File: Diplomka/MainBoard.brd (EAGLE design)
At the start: 100 x 100 mm, 44 parts, among them K1 ARK550/2, Q1 AP2012P3C-P22, Q2 BC817-40LT1SMD, Q3 SS8050-G, Q4 SS8050-G, U1 ESP32-WROOM-32, U2 AMS1117-3.3

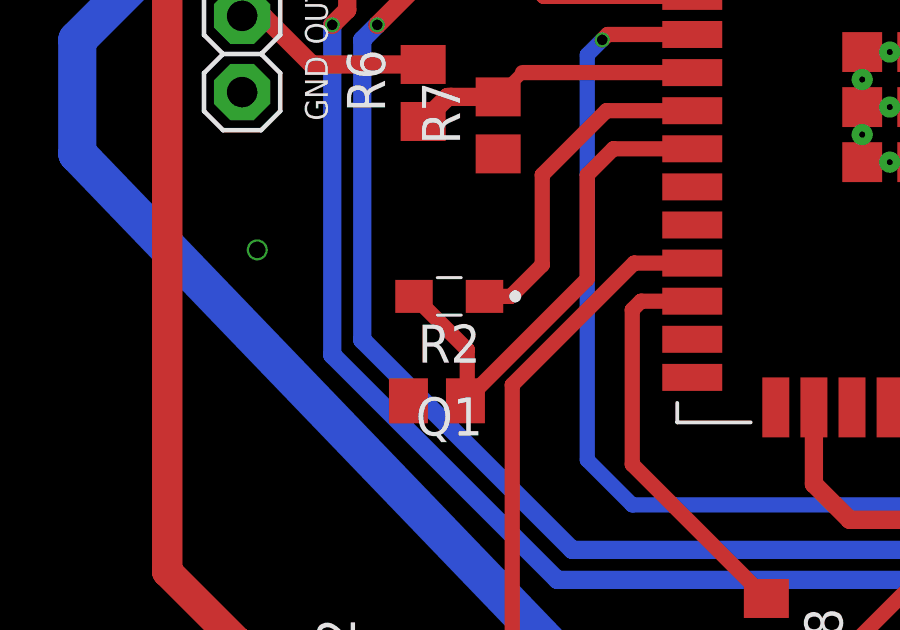
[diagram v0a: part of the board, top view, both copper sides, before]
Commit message: Přidán rozumný fototranzistor.
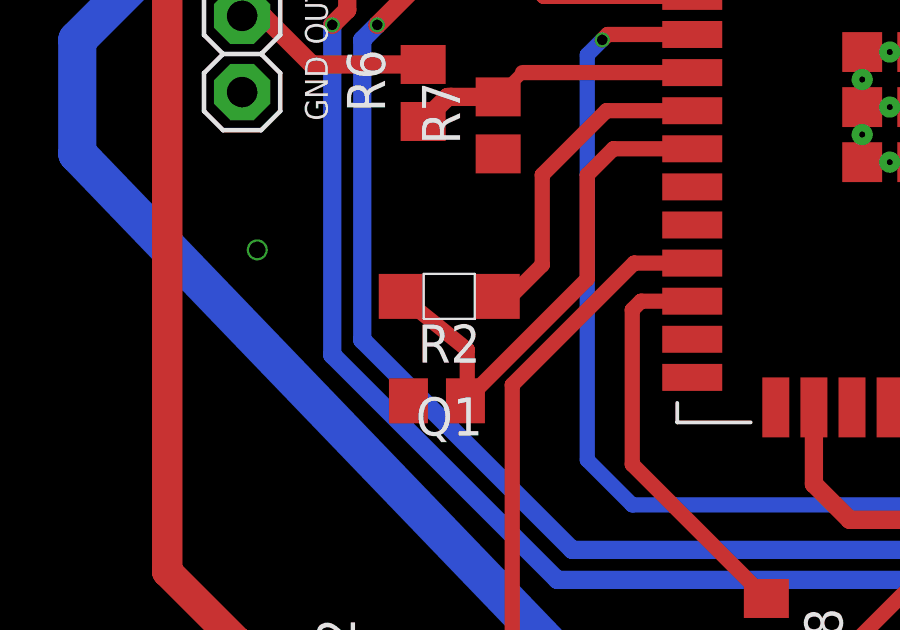
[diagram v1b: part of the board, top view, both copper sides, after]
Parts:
- Q1: value AP2012P3C-P22 -> PT15-21C/TR8; device SamacSys_Parts:AP2012P3CP22 -> myParts:PT15-21C/TR8
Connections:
- net PHOTOTRAN: now also Q1.E; no longer Q1.2
- net PHOTOTRAN_CONTROL: now also Q1.C; no longer Q1.1
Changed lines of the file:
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@@
 <grid distance="1" unitdist="mm" unit="mm" style="lines" multiple="1" display="yes" altdistance="5" altunitdist="mil" altunit="mil"/>
 <layers>
-<layer number="1" name="Top" color="4" fill="1" visible="no" active="yes"/>
+<layer number="1" name="Top" color="4" fill="1" visible="yes" active="yes"/>
 <layer number="2" name="Route2" color="1" fill="3" visible="no" active="no"/>
 <layer number="3" name="Route3" color="4" fill="3" visible="no" active="no"/>
@@
 <layer number="14" name="Route14" color="1" fill="6" visible="no" active="no"/>
 <layer number="15" name="Route15" color="4" fill="6" visible="no" active="no"/>
-<layer number="16" name="Bottom" color="1" fill="1" visible="no" active="yes"/>
+<layer number="16" name="Bottom" color="1" fill="1" visible="yes" active="yes"/>
 <layer number="17" name="Pads" color="2" fill="1" visible="yes" active="yes"/>
 <layer number="18" name="Vias" color="2" fill="1" visible="yes" active="yes"/>
@@
 <attribute name="VALUE" x="58.93" y="19.27" size="1.27" layer="27" rot="R270"/>
 </element>
-<element name="Q1" library="SamacSys_Parts" package="AP2012P3CP22" value="AP2012P3C-P22" x="33.4" y="41.45" smashed="yes" rot="R180">
-<attribute name="DESCRIPTION" value="Phototransistors 2x1.2mm PHOTOTRANS SMD LED" x="8" y="124" size="1.778" layer="27" rot="R180" display="off"/>
-<attribute name="HEIGHT" value="1.1mm" x="8" y="124" size="1.778" layer="27" rot="R180" display="off"/>
-<attribute name="MANUFACTURER_NAME" value="Kingbright" x="8" y="124" size="1.778" layer="27" rot="R180" display="off"/>
-<attribute name="MANUFACTURER_PART_NUMBER" value="AP2012P3C-P22" x="8" y="124" size="1.778" layer="27" rot="R180" display="off"/>
-<attribute name="MOUSER_PART_NUMBER" value="604-AP2012P3C-P22" x="8" y="124" size="1.778" layer="27" rot="R180" display="off"/>
-<attribute name="MOUSER_PRICE-STOCK" value="https://www.mouser.com/Search/Refine.aspx?Keyword=604-AP2012P3C-P22" x="8" y="124" size="1.778" layer="27" rot="R180" display="off"/>
+<element name="Q1" library="myParts" package="PT15-21C/TR8" value="PT15-21C/TR8" x="33.4" y="41.45" smashed="yes" rot="R180">
 <attribute name="NAME" x="33.4" y="37.45" size="1.27" layer="25" rot="R180" align="center"/>
 <attribute name="VALUE" x="33.4" y="44.45" size="1.27" layer="27" rot="R180" align="center"/>
@@
 <signal name="PHOTOTRAN">
 <contactref element="R2" pad="2"/>
-<contactref element="Q1" pad="2"/>
+<contactref element="Q1" pad="E"/>
 <contactref element="U1" pad="8"/>
 <wire x1="33.94" y1="37.97" x2="38" y2="42.03" width="0.508" layer="1"/>
@@
 <wire x1="38" y1="45.5" x2="38.87" y2="46.37" width="0.508" layer="1"/>
 <wire x1="38.87" y1="46.37" x2="41.5" y2="46.37" width="0.508" layer="1"/>
-<wire x1="32.225" y1="41.45" x2="34" y2="39.675" width="0.508" layer="1"/>
+<wire x1="31.8" y1="41.45" x2="34" y2="39.675" width="0.508" layer="1"/>
 <wire x1="34" y1="38.03" x2="33.94" y2="37.97" width="0.508" layer="1"/>
 <wire x1="34" y1="39.675" x2="34" y2="38.03" width="0.508" layer="1"/>
@@
 </signal>
 <signal name="PHOTOTRAN_CONTROL">
-<contactref element="Q1" pad="1"/>
+<contactref element="Q1" pad="C"/>
 <contactref element="U1" pad="7"/>
-<wire x1="34.575" y1="41.45" x2="34.625" y2="41.5" width="0.508" layer="1"/>
+<wire x1="35" y1="41.45" x2="34.625" y2="41.5" width="0.508" layer="1"/>
 <wire x1="41.5" y1="47.64" x2="38.64" y2="47.64" width="0.508" layer="1"/>
 <wire x1="36.5" y1="45.5" x2="36.5" y2="42.5" width="0.508" layer="1"/>
 <wire x1="36.5" y1="42.5" x2="35.45" y2="41.45" width="0.508" layer="1"/>
-<wire x1="35.45" y1="41.45" x2="34.575" y2="41.45" width="0.508" layer="1"/>
+<wire x1="35.45" y1="41.45" x2="35" y2="41.45" width="0.508" layer="1"/>
 <wire x1="38.64" y1="47.64" x2="36.5" y2="45.5" width="0.508" layer="1"/>
 </signal>
@@
 <mfgpreviewcolor name="substratecolor" color="0xFF786E46"/>
 </mfgpreviewcolors>
+<errors>
+</errors>
 </board>
 </drawing>

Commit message: Udělána objednávka.
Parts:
- Q2: value BC817-40LT1SMD -> SS8050-G; device transistor-npn:SOT23-BEC -> SS8050-G:SOT95P240X115-3N
- R16, R17: value (none) -> 10k
- moved Q2 2.00 mm to (51.4, 27.6), turned to 0 degrees
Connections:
- net GND: now also Q2.2; no longer Q2.E
- net N$1: now also Q2.3; no longer Q2.C
- net N$2: now also Q2.1; no longer Q2.B
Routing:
- net N$2: track 10.7 -> 6.71 mm
- net N$1: track 11.5 -> 10.2 mm
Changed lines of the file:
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@@
 <drawing>
 <settings>
-<setting alwaysvectorfont="yes"/>
+<setting alwaysvectorfont="no"/>
 <setting verticaltext="up"/>
 </settings>
@@
 <attribute name="VALUE" x="33.4" y="44.45" size="1.27" layer="27" rot="R180" align="center"/>
 </element>
-<element name="Q2" library="transistor-npn" library_urn="urn:adsk.eagle:library:398" package="SOT23-BEC" package3d_urn="urn:adsk.eagle:package:28748/2" value="BC817-40LT1SMD" x="51.39" y="29.58" smashed="yes" rot="R180">
-<attribute name="NAME" x="53.295" y="27.675" size="1.27" layer="25" rot="R180"/>
-<attribute name="POPULARITY" value="10" x="-21" y="88" size="1.778" layer="27" rot="R180" display="off"/>
-<attribute name="VALUE" x="53.295" y="32.755" size="1.27" layer="27" rot="R180"/>
+<element name="Q2" library="SS8050-G" package="SOT95P240X115-3N" value="SS8050-G" x="51.39" y="27.58" smashed="yes">
+<attribute name="DESCRIPTION" value="Bipolar Transistors - BJT NPN TRANSISTOR 1.5A 40V" x="51.39" y="27.58" size="1.778" layer="27" display="off"/>
+<attribute name="HEIGHT" value="1.15mm" x="51.39" y="27.58" size="1.778" layer="27" display="off"/>
+<attribute name="MANUFACTURER_NAME" value="Comchip Technology" x="51.39" y="27.58" size="1.778" layer="27" display="off"/>
+<attribute name="MANUFACTURER_PART_NUMBER" value="SS8050-G" x="51.39" y="27.58" size="1.778" layer="27" display="off"/>
+<attribute name="MOUSER_PART_NUMBER" value="750-SS8050-G" x="51.39" y="27.58" size="1.778" layer="27" display="off"/>
+<attribute name="MOUSER_PRICE-STOCK" value="https://www.mouser.co.uk/ProductDetail/Comchip-Technology/SS8050-G?qs=LLUE9lz1YbcHg%252BWLMAtcrQ%3D%3D" x="51.39" y="27.58" size="1.778" layer="27" display="off"/>
+<attribute name="NAME" x="49.485" y="29.485" size="1.27" layer="25"/>
+<attribute name="VALUE" x="49.485" y="24.405" size="1.27" layer="27"/>
 </element>
 <element name="R1" library="rcl" library_urn="urn:adsk.eagle:library:334" package="R0805" package3d_urn="urn:adsk.eagle:package:23553/2" value="1K" x="61.03" y="65.55" smashed="yes" rot="R90">
@@
 <attribute name="VALUE" x="57.5" y="31.5" size="1.27" layer="27" rot="R180" align="center"/>
 </element>
-<element name="R16" library="rcl" library_urn="urn:adsk.eagle:library:334" package="R0805" package3d_urn="urn:adsk.eagle:package:23553/2" value="" x="30" y="53" smashed="yes" rot="R90">
+<element name="R16" library="rcl" library_urn="urn:adsk.eagle:library:334" package="R0805" package3d_urn="urn:adsk.eagle:package:23553/2" value="10k" x="30" y="53" smashed="yes" rot="R90">
 <attribute name="NAME" x="28.73" y="52.365" size="1.27" layer="25" rot="R90"/>
 <attribute name="POPULARITY" value="86" x="30" y="53" size="1.778" layer="27" rot="R90" display="off"/>
@@
 <attribute name="VALUE" x="32.54" y="52.365" size="1.27" layer="27" rot="R90"/>
 </element>
-<element name="R17" library="rcl" library_urn="urn:adsk.eagle:library:334" package="R0805" package3d_urn="urn:adsk.eagle:package:23553/2" value="" x="67.5" y="26.5" smashed="yes" rot="R90">
+<element name="R17" library="rcl" library_urn="urn:adsk.eagle:library:334" package="R0805" package3d_urn="urn:adsk.eagle:package:23553/2" value="10k" x="67.5" y="26.5" smashed="yes" rot="R90">
 <attribute name="NAME" x="66.23" y="25.865" size="1.27" layer="25" rot="R90"/>
 <attribute name="POPULARITY" value="86" x="67.5" y="26.5" size="1.778" layer="27" rot="R90" display="off"/>
@@
 <contactref element="R5" pad="1"/>
 <contactref element="U$3" pad="GND"/>
-<contactref element="Q2" pad="E"/>
+<contactref element="Q2" pad="2"/>
 <contactref element="LED1" pad="C"/>
 <contactref element="U$5" pad="GND"/>
@@
 </signal>
 <signal name="N$1">
-<contactref element="Q2" pad="C"/>
+<contactref element="Q2" pad="3"/>
 <contactref element="U$4" pad="-"/>
-<wire x1="53.8" y1="17.96" x2="51.39" y2="20.37" width="1.27" layer="1"/>
-<wire x1="51.39" y1="20.37" x2="51.39" y2="28.48" width="1.27" layer="1"/>
+<wire x1="53.8" y1="17.96" x2="53.8" y2="26.27" width="1.27" layer="1"/>
+<wire x1="53.8" y1="26.27" x2="52.49" y2="27.58" width="1.27" layer="1"/>
 </signal>
 <signal name="N$2">
 <contactref element="R8" pad="2"/>
-<contactref element="Q2" pad="B"/>
-<wire x1="52.34" y1="30.68" x2="52.34" y2="31.16" width="0.508" layer="1"/>
-<wire x1="52.34" y1="31.16" x2="51" y2="32.5" width="0.508" layer="1"/>
-<wire x1="51" y1="32.5" x2="49.5" y2="32.5" width="0.508" layer="1"/>
-<wire x1="46.48" y1="29.48" x2="43.97" y2="29.48" width="0.508" layer="1"/>
-<wire x1="49.5" y1="32.5" x2="46.48" y2="29.48" width="0.508" layer="1"/>
+<contactref element="Q2" pad="1"/>
+<wire x1="43.97" y1="29.48" x2="49.34" y2="29.48" width="0.4064" layer="1"/>
+<wire x1="49.34" y1="29.48" x2="50.29" y2="28.53" width="0.4064" layer="1"/>
 </signal>
 <signal name="N$5">
